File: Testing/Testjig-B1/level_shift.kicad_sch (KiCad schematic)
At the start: 6 parts, among them U6 74HC14, U7 74HC14

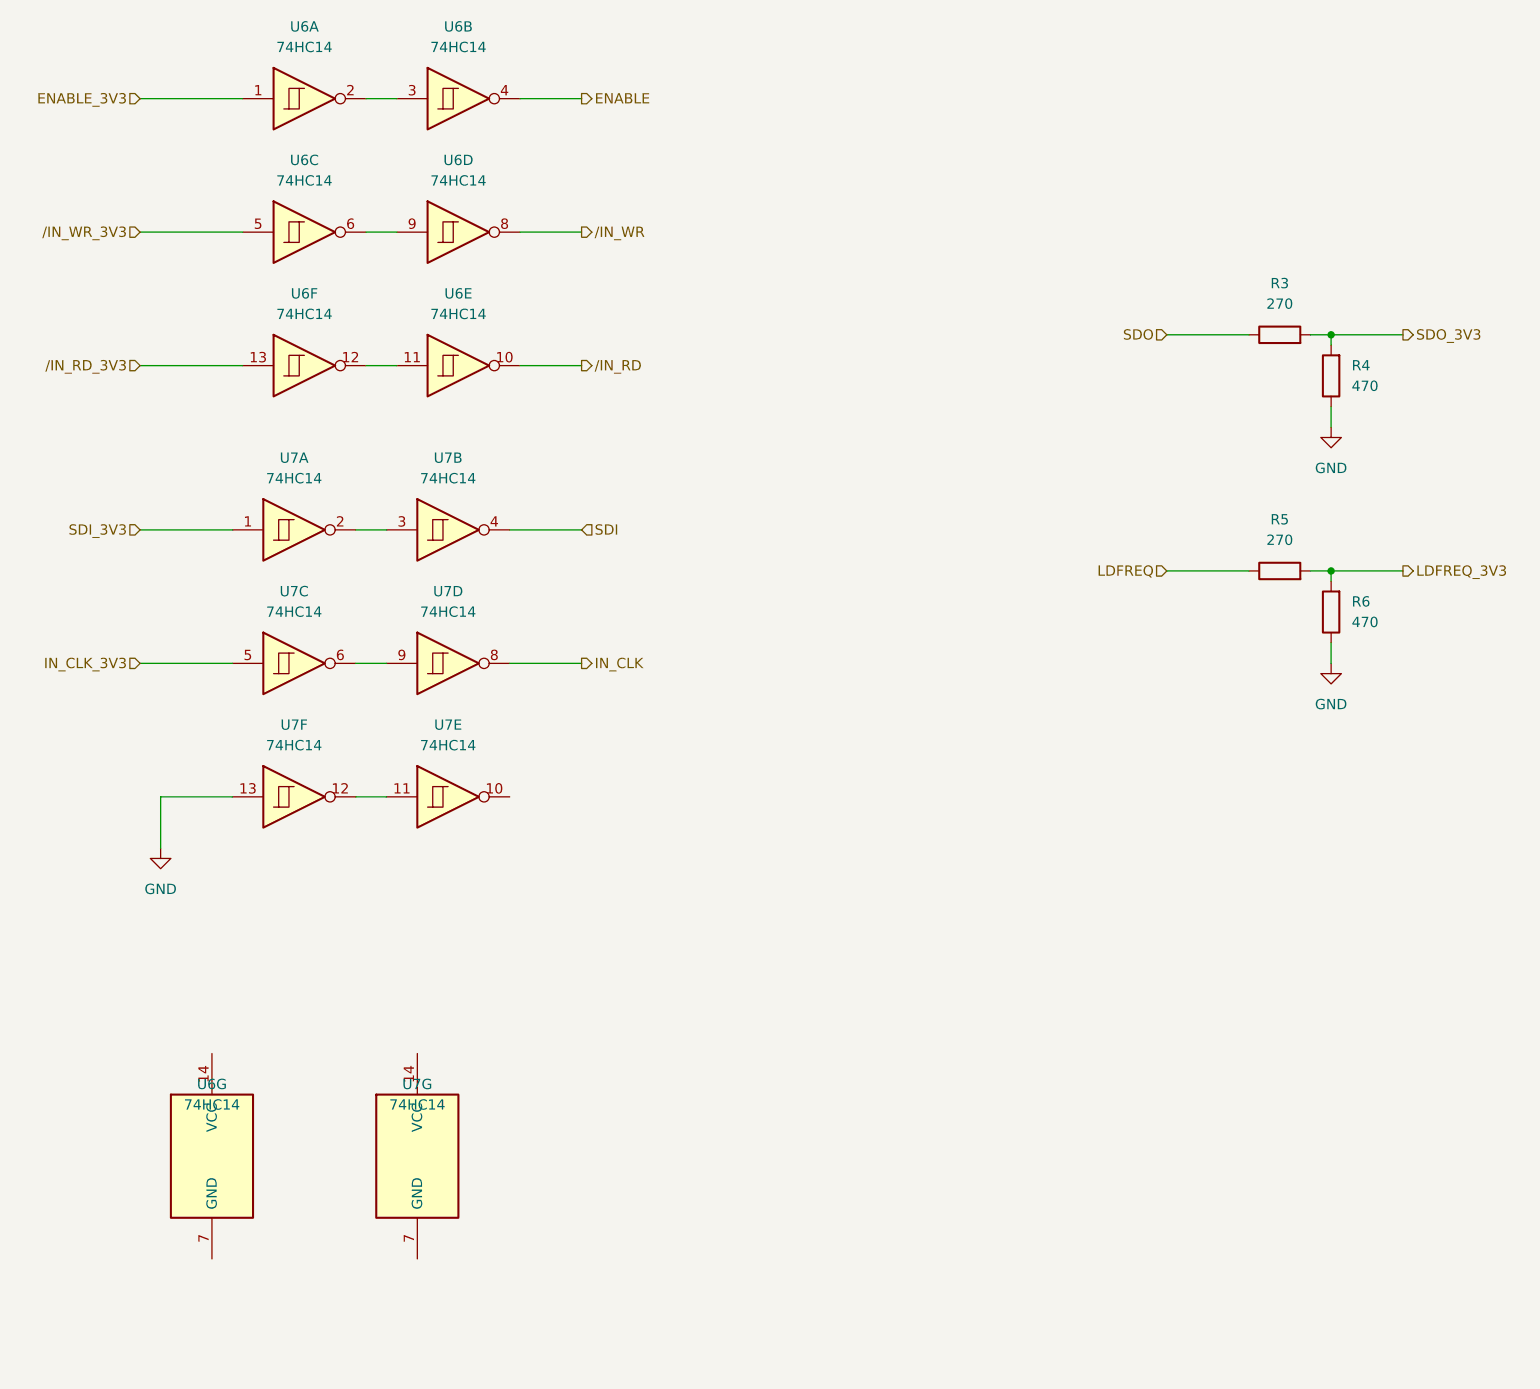
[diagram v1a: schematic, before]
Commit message: First iteration tester design
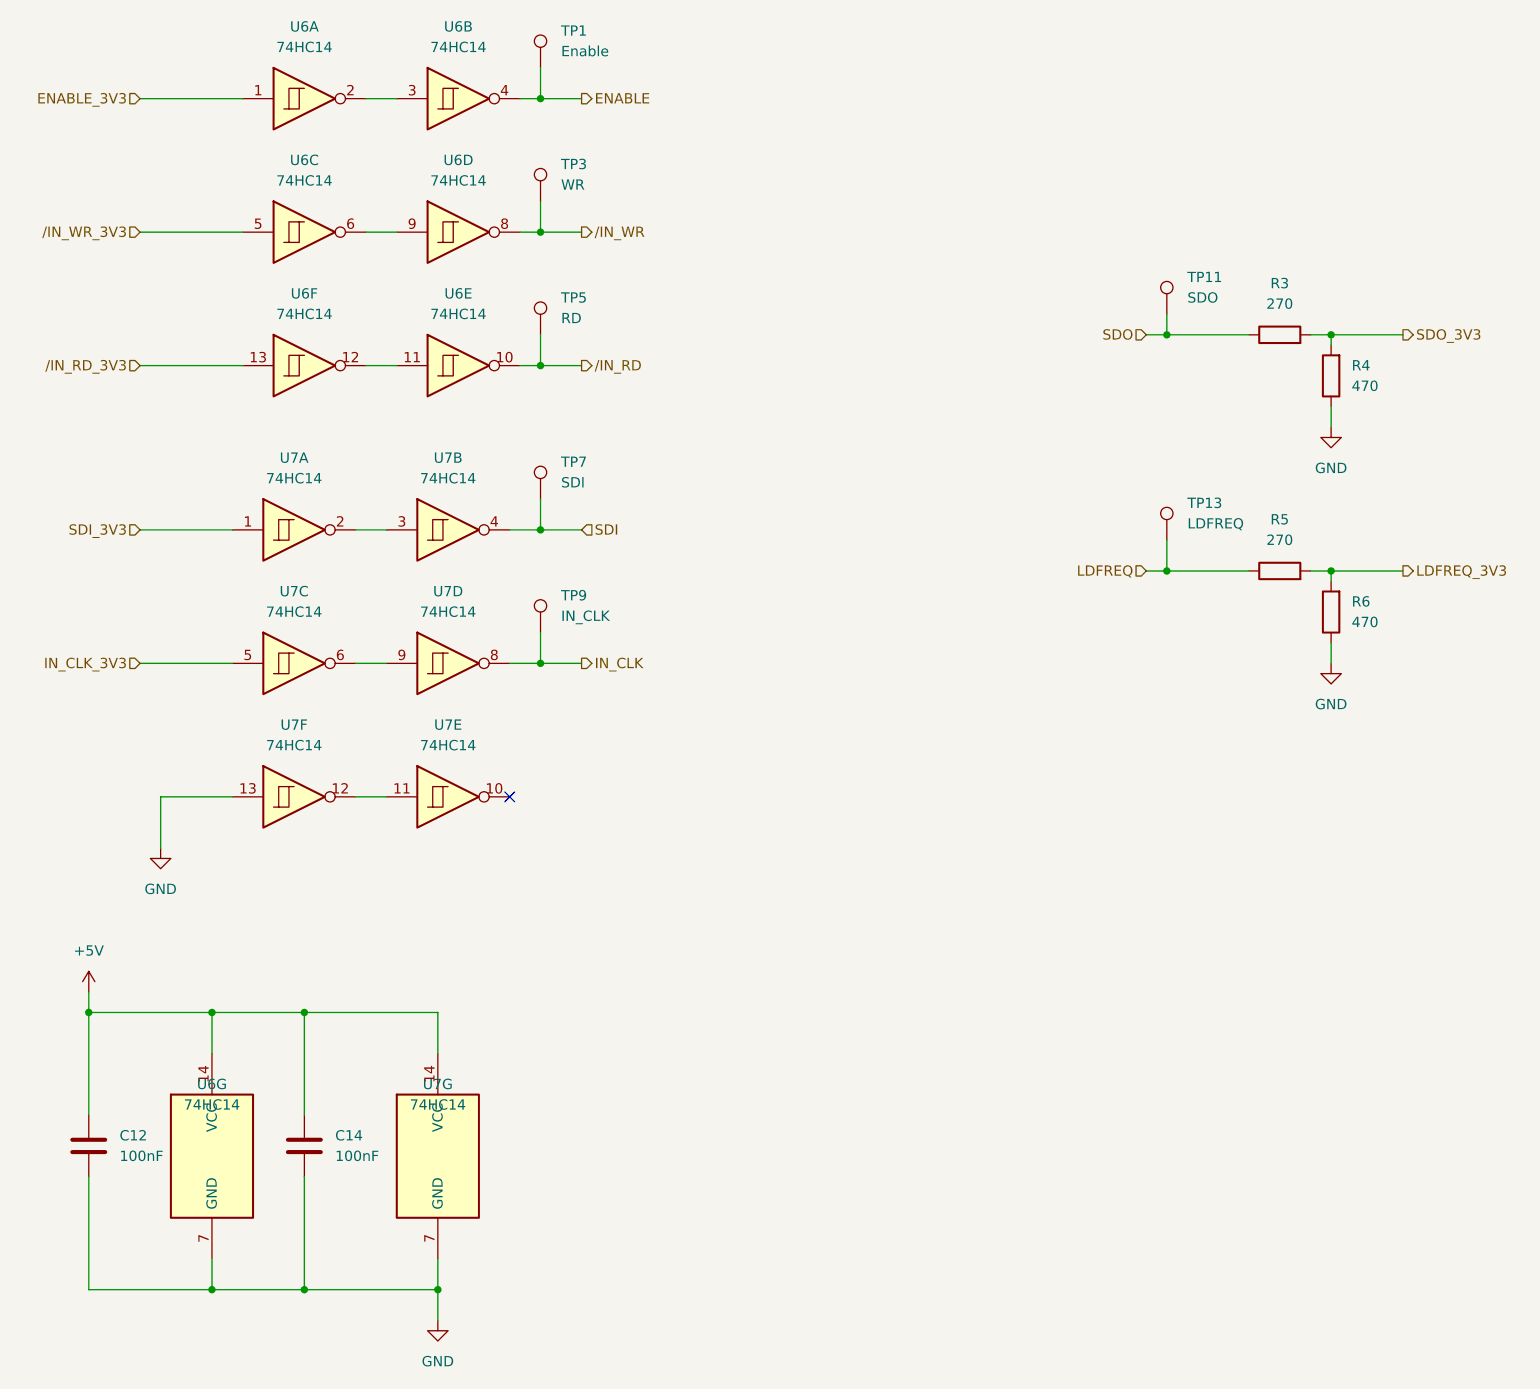
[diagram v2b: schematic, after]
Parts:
- added C12, C14: 100nF, Capacitor_SMD:C_0805_2012Metric_Pad1.18x1.45mm_HandSolder, symbol Device:C
- added TP1: Enable, TestPoint:TestPoint_Loop_D2.60mm_Drill1.4mm_Beaded, symbol Connector:TestPoint
- added TP11: SDO, TestPoint:TestPoint_Loop_D2.60mm_Drill1.4mm_Beaded, symbol Connector:TestPoint
- added TP13: LDFREQ, TestPoint:TestPoint_Loop_D2.60mm_Drill1.4mm_Beaded, symbol Connector:TestPoint
- added TP3: WR, TestPoint:TestPoint_Loop_D2.60mm_Drill1.4mm_Beaded, symbol Connector:TestPoint
- added TP5: RD, TestPoint:TestPoint_Loop_D2.60mm_Drill1.4mm_Beaded, symbol Connector:TestPoint
- added TP7: SDI, TestPoint:TestPoint_Loop_D2.60mm_Drill1.4mm_Beaded, symbol Connector:TestPoint
- added TP9: IN_CLK, TestPoint:TestPoint_Loop_D2.60mm_Drill1.4mm_Beaded, symbol Connector:TestPoint
- R3, R4, R5, R6: footprint (none) -> Resistor_SMD:R_0805_2012Metric
- U6, U7: footprint (none) -> Package_SO:SOIC-14_3.9x8.7mm_P1.27mm
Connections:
- net ENABLE: now also TP1.1
- net GND: now also U6.7 (GND), U7.7 (GND), C12.2, C14.2
- net IN_CLK: now also TP9.1
- net LDFREQ: now also TP13.1
- net SDI: now also TP7.1
- net SDO: now also TP11.1
- net /IN_RD: now also TP5.1
- net /IN_WR: now also TP3.1
- net +5V: now reaches U7.14 (VCC)
- net +5V: now also U6.14 (VCC), C12.1, C14.1
- no-connect marks 0 -> 1
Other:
- moved on the sheet: U7G
